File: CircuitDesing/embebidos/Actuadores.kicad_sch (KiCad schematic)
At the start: 18 parts, among them Q1 IRF540N, Q2 IRF540N, Q3 IRF540N

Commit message: Todas las huellas
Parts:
- D10, D6, D8: footprint (none) -> LED_SMD:LED_0603_1608Metric_Pad1.05x0.95mm_HandSolder
- Vent1, Vent2: footprint (none) -> Connector_JST:JST_EH_B2B-EH-A_1x02_P2.50mm_Vertical
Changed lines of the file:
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@@
       (effects (font (size 1.27 1.27)) (justify right))
     )
-    (property "Footprint" "" (id 2) (at 147.32 114.3 0)
+    (property "Footprint" "LED_SMD:LED_0603_1608Metric_Pad1.05x0.95mm_HandSolder" (id 2) (at 147.32 114.3 0)
       (effects (font (size 1.27 1.27)) hide)
     )
@@
     (property "Reference" "Vent2" (id 0) (at 151.13 77.47 0))
     (property "Value" "Conn_01x02" (id 1) (at 151.13 80.01 0))
-    (property "Footprint" "" (id 2) (at 151.13 86.36 0)
+    (property "Footprint" "Connector_JST:JST_EH_B2B-EH-A_1x02_P2.50mm_Vertical" (id 2) (at 151.13 86.36 0)
       (effects (font (size 1.27 1.27)) hide)
     )
@@
       (effects (font (size 1.27 1.27)) (justify right))
     )
-    (property "Footprint" "" (id 2) (at 87.63 114.3 0)
+    (property "Footprint" "LED_SMD:LED_0603_1608Metric_Pad1.05x0.95mm_HandSolder" (id 2) (at 87.63 114.3 0)
       (effects (font (size 1.27 1.27)) hide)
     )
@@
     (property "Reference" "Vent1" (id 0) (at 91.44 77.47 0))
     (property "Value" "Conn_01x02" (id 1) (at 91.44 80.01 0))
-    (property "Footprint" "" (id 2) (at 91.44 86.36 0)
+    (property "Footprint" "Connector_JST:JST_EH_B2B-EH-A_1x02_P2.50mm_Vertical" (id 2) (at 91.44 86.36 0)
       (effects (font (size 1.27 1.27)) hide)
     )
@@
       (effects (font (size 1.27 1.27)) (justify right))
     )
-    (property "Footprint" "" (id 2) (at 205.74 114.3 0)
+    (property "Footprint" "LED_SMD:LED_0603_1608Metric_Pad1.05x0.95mm_HandSolder" (id 2) (at 205.74 114.3 0)
       (effects (font (size 1.27 1.27)) hide)
     )

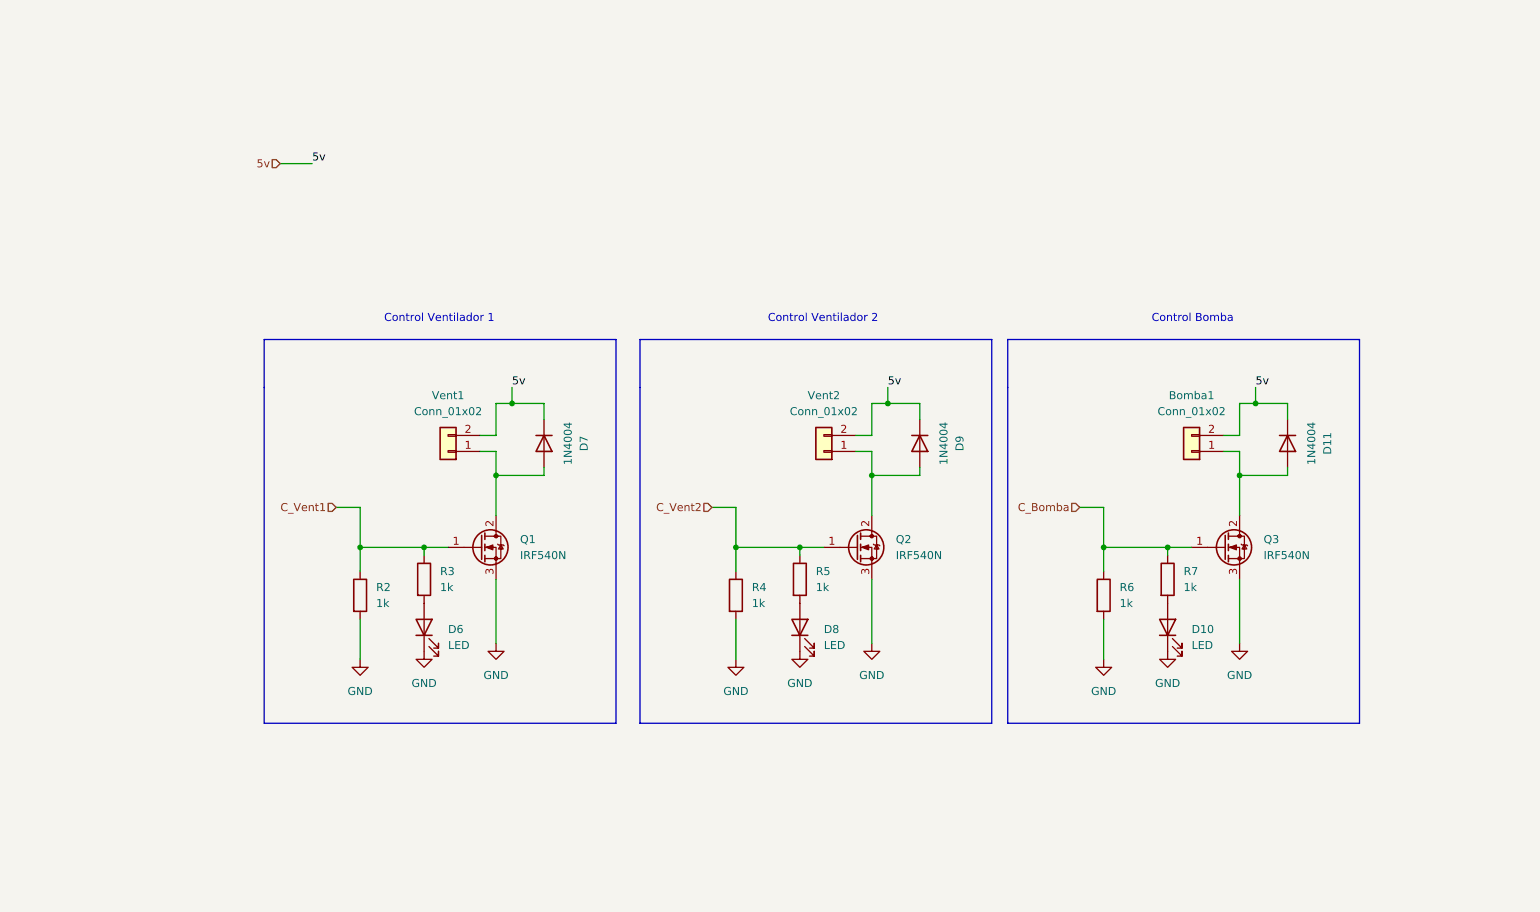
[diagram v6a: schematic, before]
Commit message: Coversores lógicos + alertas + humidificador
Coversores lógicos + alertas + humidificador
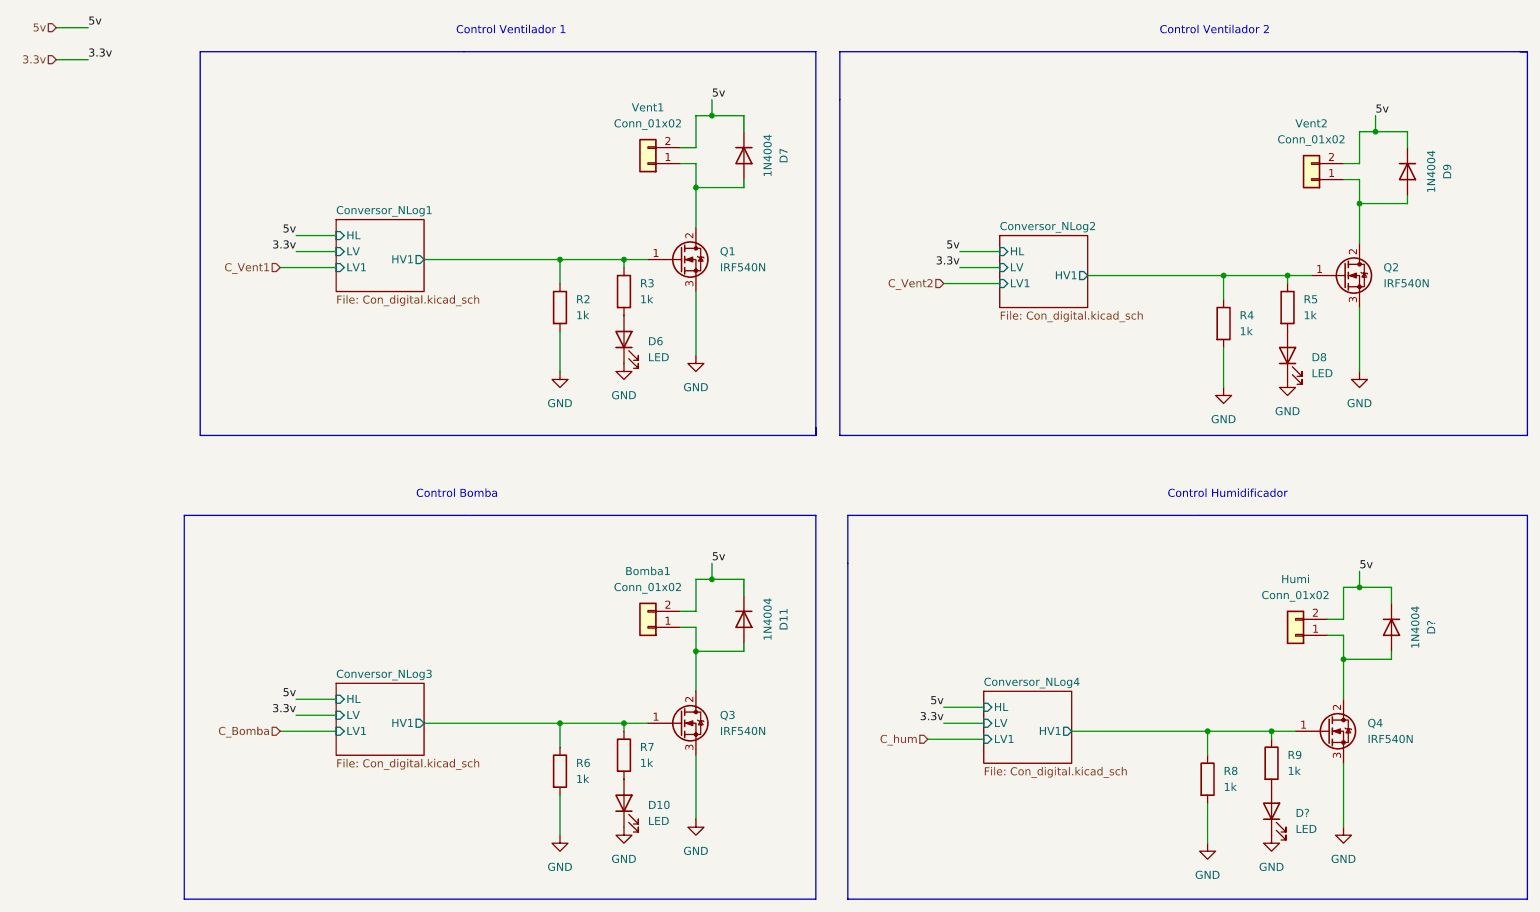
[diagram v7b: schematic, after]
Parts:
- added D?: LED, LED_SMD:LED_0603_1608Metric_Pad1.05x0.95mm_HandSolder, symbol Device:LED
- added D?: 1N4004, Diode_THT:D_DO-41_SOD81_P10.16mm_Horizontal, symbol Diode:1N4004
- added Humi: Conn_01x02, Connector_JST:JST_EH_B2B-EH-A_1x02_P2.50mm_Vertical, symbol Connector_Generic:Conn_01x02
- added Q4: IRF540N, Package_TO_SOT_THT:TO-220-3_Vertical, symbol Transistor_FET:IRF540N
- added R8, R9: 1k, Resistor_SMD:R_0603_1608Metric_Pad0.98x0.95mm_HandSolder, symbol Device:R
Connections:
- net 5v: now also D?.1 (K), Humi.2 (Pin_2)
- net C_Bomba: no longer Q3.1 (G), R6.1, R7.1
- net C_Vent1: no longer Q1.1 (G), R2.1, R3.1
- net C_Vent2: no longer Q2.1 (G), R4.1, R5.1
- net GND: now also D?.1 (K), Q4.3 (S), R8.2
- new net: D?.2 (A), R9.2
- new net: D?.2 (A), Humi.1 (Pin_1), Q4.2 (D)
- new net Conversor_NLog1/HV1: Q1.1 (G), R2.1, R3.1
- new net Conversor_NLog2/HV1: Q2.1 (G), R4.1, R5.1
- new net Conversor_NLog3/HV1: Q3.1 (G), R6.1, R7.1
- new net Conversor_NLog4/HV1: Q4.1 (G), R8.1, R9.1
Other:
- added sheet Conversor_NLog1 (Con_digital.kicad_sch)
- added sheet Conversor_NLog2 (Con_digital.kicad_sch)
- added sheet Conversor_NLog3 (Con_digital.kicad_sch)
- added sheet Conversor_NLog4 (Con_digital.kicad_sch)
- note added: "Control Humidificador"
- moved on the sheet: Bomba1, D10, D11, D6, D7, D8, D9, Q1, Q2, Q3, R2, R3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

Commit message: Ruteo completo
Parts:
- gave numbers to parts that had none: 2
- renumbered D6 to D1, D10 to D2, D7 to D3, D11 to D4, D8 to D6, D9 to D8, Humi to Humi1, Q1 to Q2, Q2 to Q5, R5 to R10, R2 to R3, R6 to R4, R3 to R5, R7 to R6, R8 to R7, R4 to R8
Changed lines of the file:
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@@
   (symbol (lib_id "Device:R") (at 119.38 60.96 0) (unit 1)
     (in_bom yes) (on_board yes) (fields_autoplaced)
-    (property "Reference" "R3" (id 0) (at 121.92 59.6899 0)
+    (property "Reference" "R5" (id 0) (at 121.92 59.6899 0)
       (effects (font (size 1.27 1.27)) (justify left))
     )
@@
   (symbol (lib_id "Device:LED") (at 224.79 71.12 90) (unit 1)
     (in_bom yes) (on_board yes) (fields_autoplaced)
-    (property "Reference" "D8" (id 0) (at 228.6 71.4374 90)
+    (property "Reference" "D6" (id 0) (at 228.6 71.4374 90)
       (effects (font (size 1.27 1.27)) (justify right))
     )
@@
   (symbol (lib_id "Device:R") (at 212.09 138.43 0) (unit 1)
     (in_bom yes) (on_board yes) (fields_autoplaced)
-    (property "Reference" "R8" (id 0) (at 214.63 137.1599 0)
+    (property "Reference" "R7" (id 0) (at 214.63 137.1599 0)
       (effects (font (size 1.27 1.27)) (justify left))
     )
@@
   (symbol (lib_id "Device:R") (at 109.22 63.5 0) (unit 1)
     (in_bom yes) (on_board yes) (fields_autoplaced)
-    (property "Reference" "R2" (id 0) (at 111.76 62.2299 0)
+    (property "Reference" "R3" (id 0) (at 111.76 62.2299 0)
       (effects (font (size 1.27 1.27)) (justify left))
     )
@@
   (symbol (lib_id "Transistor_FET:IRF540N") (at 128.27 55.88 0) (unit 1)
     (in_bom yes) (on_board yes) (fields_autoplaced)
-    (property "Reference" "Q1" (id 0) (at 134.62 54.6099 0)
+    (property "Reference" "Q2" (id 0) (at 134.62 54.6099 0)
       (effects (font (size 1.27 1.27)) (justify left))
     )
@@
   (symbol (lib_id "Device:LED") (at 222.25 143.51 90) (unit 1)
     (in_bom yes) (on_board yes) (fields_autoplaced)
-    (property "Reference" "D?" (id 0) (at 226.06 143.8274 90)
+    (property "Reference" "D5" (id 0) (at 226.06 143.8274 90)
       (effects (font (size 1.27 1.27)) (justify right))
     )
@@
   (symbol (lib_id "Device:LED") (at 119.38 68.58 90) (unit 1)
     (in_bom yes) (on_board yes) (fields_autoplaced)
-    (property "Reference" "D6" (id 0) (at 123.19 68.8974 90)
+    (property "Reference" "D1" (id 0) (at 123.19 68.8974 90)
       (effects (font (size 1.27 1.27)) (justify right))
     )
@@
   (symbol (lib_id "power:GND") (at 222.25 147.32 0) (unit 1)
     (in_bom yes) (on_board yes) (fields_autoplaced)
-    (property "Reference" "#PWR?" (id 0) (at 222.25 153.67 0)
+    (property "Reference" "#PWR024" (id 0) (at 222.25 153.67 0)
       (effects (font (size 1.27 1.27)) hide)
     )
@@
   (symbol (lib_id "power:GND") (at 214.63 76.2 0) (unit 1)
     (in_bom yes) (on_board yes) (fields_autoplaced)
-    (property "Reference" "#PWR010" (id 0) (at 214.63 82.55 0)
+    (property "Reference" "#PWR023" (id 0) (at 214.63 82.55 0)
       (effects (font (size 1.27 1.27)) hide)
     )
@@
   (symbol (lib_id "power:GND") (at 224.79 74.93 0) (unit 1)
     (in_bom yes) (on_board yes) (fields_autoplaced)
-    (property "Reference" "#PWR011" (id 0) (at 224.79 81.28 0)
+    (property "Reference" "#PWR025" (id 0) (at 224.79 81.28 0)
       (effects (font (size 1.27 1.27)) hide)
     )
@@
   (symbol (lib_id "Device:LED") (at 119.38 142.24 90) (unit 1)
     (in_bom yes) (on_board yes) (fields_autoplaced)
-    (property "Reference" "D10" (id 0) (at 123.19 142.5574 90)
+    (property "Reference" "D2" (id 0) (at 123.19 142.5574 90)
       (effects (font (size 1.27 1.27)) (justify right))
     )
@@
   (symbol (lib_id "Connector_Generic:Conn_01x02") (at 226.06 115.57 180) (unit 1)
     (in_bom yes) (on_board yes) (fields_autoplaced)
-    (property "Reference" "Humi" (id 0) (at 226.06 106.68 0))
+    (property "Reference" "Humi1" (id 0) (at 226.06 106.68 0))
     (property "Value" "Conn_01x02" (id 1) (at 226.06 109.22 0))
     (property "Footprint" "Connector_JST:JST_EH_B2B-EH-A_1x02_P2.50mm_Vertical" (id 2) (at 226.06 115.57 0)
@@
   (symbol (lib_id "power:GND") (at 119.38 72.39 0) (unit 1)
     (in_bom yes) (on_board yes) (fields_autoplaced)
-    (property "Reference" "#PWR08" (id 0) (at 119.38 78.74 0)
+    (property "Reference" "#PWR018" (id 0) (at 119.38 78.74 0)
       (effects (font (size 1.27 1.27)) hide)
     )
@@
   (symbol (lib_id "power:GND") (at 119.38 146.05 0) (unit 1)
     (in_bom yes) (on_board yes) (fields_autoplaced)
-    (property "Reference" "#PWR014" (id 0) (at 119.38 152.4 0)
+    (property "Reference" "#PWR019" (id 0) (at 119.38 152.4 0)
       (effects (font (size 1.27 1.27)) hide)
     )
@@
   (symbol (lib_id "power:GND") (at 236.22 73.66 0) (unit 1)
     (in_bom yes) (on_board yes) (fields_autoplaced)
-    (property "Reference" "#PWR012" (id 0) (at 236.22 80.01 0)
+    (property "Reference" "#PWR027" (id 0) (at 236.22 80.01 0)
       (effects (font (size 1.27 1.27)) hide)
     )
@@
   (symbol (lib_id "Transistor_FET:IRF540N") (at 233.68 58.42 0) (unit 1)
     (in_bom yes) (on_board yes) (fields_autoplaced)
-    (property "Reference" "Q2" (id 0) (at 240.03 57.1499 0)
+    (property "Reference" "Q5" (id 0) (at 240.03 57.1499 0)
       (effects (font (size 1.27 1.27)) (justify left))
     )
@@
   (symbol (lib_id "Device:R") (at 214.63 66.04 0) (unit 1)
     (in_bom yes) (on_board yes) (fields_autoplaced)
-    (property "Reference" "R4" (id 0) (at 217.17 64.7699 0)
+    (property "Reference" "R8" (id 0) (at 217.17 64.7699 0)
       (effects (font (size 1.27 1.27)) (justify left))
     )
@@
   (symbol (lib_id "Device:R") (at 109.22 137.16 0) (unit 1)
     (in_bom yes) (on_board yes) (fields_autoplaced)
-    (property "Reference" "R6" (id 0) (at 111.76 135.8899 0)
+    (property "Reference" "R4" (id 0) (at 111.76 135.8899 0)
       (effects (font (size 1.27 1.27)) (justify left))
     )
@@
   (symbol (lib_id "power:GND") (at 233.68 146.05 0) (unit 1)
     (in_bom yes) (on_board yes) (fields_autoplaced)
-    (property "Reference" "#PWR?" (id 0) (at 233.68 152.4 0)
+    (property "Reference" "#PWR026" (id 0) (at 233.68 152.4 0)
       (effects (font (size 1.27 1.27)) hide)
     )
@@
   (symbol (lib_id "Diode:1N4004") (at 243.84 41.91 270) (unit 1)
     (in_bom yes) (on_board yes) (fields_autoplaced)
-    (property "Reference" "D9" (id 0) (at 250.19 41.91 0))
+    (property "Reference" "D8" (id 0) (at 250.19 41.91 0))
     (property "Value" "1N4004" (id 1) (at 247.65 41.91 0))
     (property "Footprint" "Diode_THT:D_DO-41_SOD81_P10.16mm_Horizontal" (id 2) (at 239.395 41.91 0)
@@
   (symbol (lib_id "Device:R") (at 224.79 63.5 0) (unit 1)
     (in_bom yes) (on_board yes) (fields_autoplaced)
-    (property "Reference" "R5" (id 0) (at 227.33 62.2299 0)
+    (property "Reference" "R10" (id 0) (at 227.33 62.2299 0)
       (effects (font (size 1.27 1.27)) (justify left))
     )
@@
   (symbol (lib_id "Device:R") (at 119.38 134.62 0) (unit 1)
     (in_bom yes) (on_board yes) (fields_autoplaced)
-    (property "Reference" "R7" (id 0) (at 121.92 133.3499 0)
+    (property "Reference" "R6" (id 0) (at 121.92 133.3499 0)
       (effects (font (size 1.27 1.27)) (justify left))
     )
@@
   (symbol (lib_id "power:GND") (at 109.22 147.32 0) (unit 1)
     (in_bom yes) (on_board yes) (fields_autoplaced)
-    (property "Reference" "#PWR013" (id 0) (at 109.22 153.67 0)
+    (property "Reference" "#PWR017" (id 0) (at 109.22 153.67 0)
       (effects (font (size 1.27 1.27)) hide)
     )
@@
   (symbol (lib_id "power:GND") (at 130.81 71.12 0) (unit 1)
     (in_bom yes) (on_board yes) (fields_autoplaced)
-    (property "Reference" "#PWR09" (id 0) (at 130.81 77.47 0)
+    (property "Reference" "#PWR020" (id 0) (at 130.81 77.47 0)
       (effects (font (size 1.27 1.27)) hide)
     )
@@
   (symbol (lib_id "Diode:1N4004") (at 138.43 113.03 270) (unit 1)
     (in_bom yes) (on_board yes) (fields_autoplaced)
-    (property "Reference" "D11" (id 0) (at 144.78 113.03 0))
+    (property "Reference" "D4" (id 0) (at 144.78 113.03 0))
     (property "Value" "1N4004" (id 1) (at 142.24 113.03 0))
     (property "Footprint" "Diode_THT:D_DO-41_SOD81_P10.16mm_Horizontal" (id 2) (at 133.985 113.03 0)
@@
   (symbol (lib_id "Diode:1N4004") (at 241.3 114.3 270) (unit 1)
     (in_bom yes) (on_board yes) (fields_autoplaced)
-    (property "Reference" "D?" (id 0) (at 247.65 114.3 0))
+    (property "Reference" "D7" (id 0) (at 247.65 114.3 0))
     (property "Value" "1N4004" (id 1) (at 245.11 114.3 0))
     (property "Footprint" "Diode_THT:D_DO-41_SOD81_P10.16mm_Horizontal" (id 2) (at 236.855 114.3 0)
@@
   (symbol (lib_id "power:GND") (at 212.09 148.59 0) (unit 1)
     (in_bom yes) (on_board yes) (fields_autoplaced)
-    (property "Reference" "#PWR?" (id 0) (at 212.09 154.94 0)
+    (property "Reference" "#PWR022" (id 0) (at 212.09 154.94 0)
       (effects (font (size 1.27 1.27)) hide)
     )
@@
   (symbol (lib_id "Diode:1N4004") (at 138.43 39.37 270) (unit 1)
     (in_bom yes) (on_board yes) (fields_autoplaced)
-    (property "Reference" "D7" (id 0) (at 144.78 39.37 0))
+    (property "Reference" "D3" (id 0) (at 144.78 39.37 0))
     (property "Value" "1N4004" (id 1) (at 142.24 39.37 0))
     (property "Footprint" "Diode_THT:D_DO-41_SOD81_P10.16mm_Horizontal" (id 2) (at 133.985 39.37 0)
@@
   (symbol (lib_id "power:GND") (at 109.22 73.66 0) (unit 1)
     (in_bom yes) (on_board yes) (fields_autoplaced)
-    (property "Reference" "#PWR07" (id 0) (at 109.22 80.01 0)
+    (property "Reference" "#PWR016" (id 0) (at 109.22 80.01 0)
       (effects (font (size 1.27 1.27)) hide)
     )
@@
   (symbol (lib_id "power:GND") (at 130.81 144.78 0) (unit 1)
     (in_bom yes) (on_board yes) (fields_autoplaced)
-    (property "Reference" "#PWR015" (id 0) (at 130.81 151.13 0)
-      (effects (font (size 1.27 1.27)) hide)
-    )
+    (property "Reference" "#PWR021" (id 0) (at 130.81 151.13 0)
+      (effects (font (size 1.27 1.27)) hide)
+    )
